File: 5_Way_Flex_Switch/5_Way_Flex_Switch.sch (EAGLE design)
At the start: 9 parts

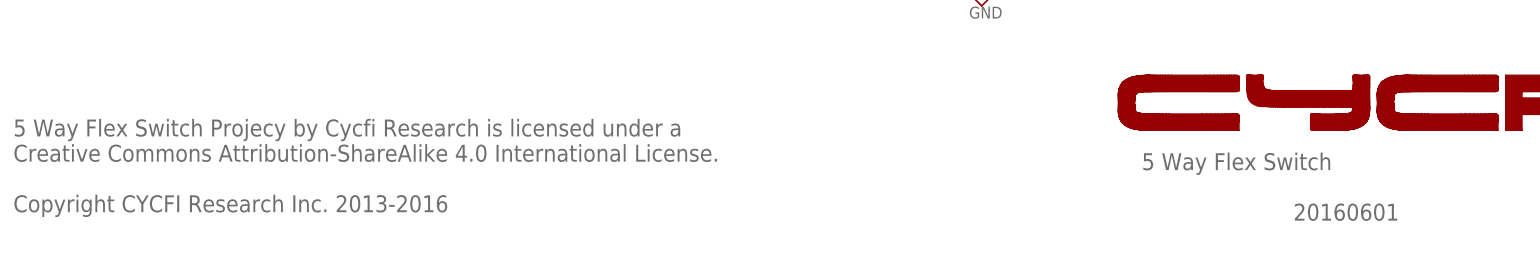
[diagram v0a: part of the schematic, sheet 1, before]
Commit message: *organize 5-waay switch and its configuration board(a and b) *update license date *remove red frame schem pdf files, change with black frame *update document number
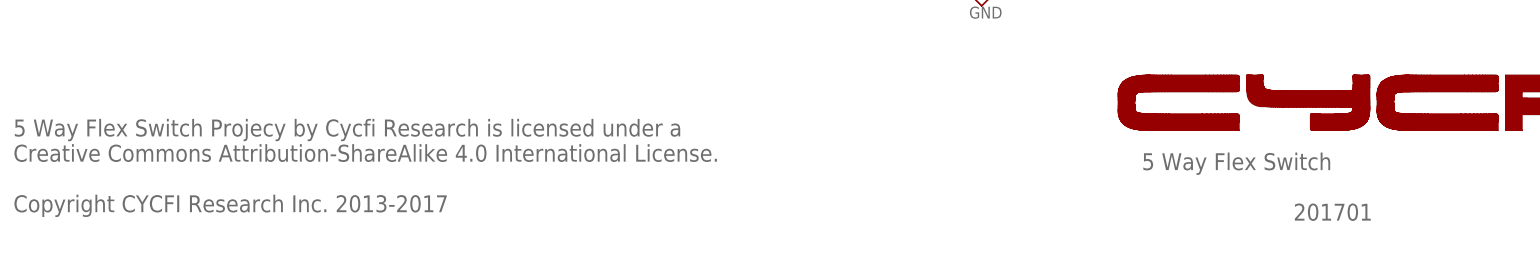
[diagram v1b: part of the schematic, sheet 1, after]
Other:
- note added: "201701"
- note added: "201702"
- note added: "5 Way Flex Switch Projecy by Cycfi Research is licensed under a Creative Commons Attribution-ShareAlike 4.0 International License. Copyright CYCFI Research Inc. 2013-2017"
- note removed: "2016037"
- note removed: "20160601"
- note removed: "5 Way Flex Switch Projecy by Cycfi Research is licensed under a Creative Commons Attribution-ShareAlike 4.0 International License. Copyright CYCFI Research Inc. 2013-2016"
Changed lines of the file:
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@@
 <text x="7.62" y="12.7" size="2.54" layer="95">5 Way Flex Switch Projecy by Cycfi Research is licensed under a
 Creative Commons Attribution-ShareAlike 4.0 International License.
-Copyright CYCFI Research Inc. 2013-2016</text>
-<text x="200.66" y="11.43" size="2.54" layer="95">20160601</text>
+Copyright CYCFI Research Inc. 2013-2017</text>
+<text x="200.66" y="11.43" size="2.54" layer="95">201701</text>
 <wire x1="192.47528125" y1="25.047221875" x2="190.115640625" y2="25.047221875" width="0" layer="94"/>
 <wire x1="190.115640625" y1="25.047221875" x2="188.10833125" y2="25.047225" width="0" layer="94"/>
@@
 <text x="7.62" y="12.7" size="2.54" layer="95">5 Way Flex Switch Projecy by Cycfi Research is licensed under a
 Creative Commons Attribution-ShareAlike 4.0 International License.
-Copyright CYCFI Research Inc. 2013-2016</text>
-<text x="200.66" y="11.43" size="2.54" layer="95">2016037</text>
+Copyright CYCFI Research Inc. 2013-2017</text>
+<text x="200.66" y="11.43" size="2.54" layer="95">201702</text>
 <wire x1="192.47528125" y1="25.047221875" x2="190.115640625" y2="25.047221875" width="0" layer="94"/>
 <wire x1="190.115640625" y1="25.047221875" x2="188.10833125" y2="25.047225" width="0" layer="94"/>

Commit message: * correct misspelled word
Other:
- note added: "5 Way Flex Switch Project by Cycfi Research is licensed under a Creative Commons Attribution-ShareAlike 4.0 International License. Copyright CYCFI Research Inc. 2013-2017"
- note removed: "5 Way Flex Switch Projecy by Cycfi Research is licensed under a Creative Commons Attribution-ShareAlike 4.0 International License. Copyright CYCFI Research Inc. 2013-2017"
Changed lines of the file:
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@@
 <text x="177.8" y="19.05" size="2.54" layer="95">5 Way Flex Switch</text>
 <text x="252.73" y="6.985" size="2.1844" layer="95">v1.2</text>
-<text x="7.62" y="12.7" size="2.54" layer="95">5 Way Flex Switch Projecy by Cycfi Research is licensed under a
+<text x="7.62" y="12.7" size="2.54" layer="95">5 Way Flex Switch Project by Cycfi Research is licensed under a
 Creative Commons Attribution-ShareAlike 4.0 International License.
 Copyright CYCFI Research Inc. 2013-2017</text>
@@
 <text x="177.8" y="19.05" size="2.54" layer="95">5 Way Flex Switch</text>
 <text x="252.73" y="6.985" size="2.1844" layer="95">v1.1</text>
-<text x="7.62" y="12.7" size="2.54" layer="95">5 Way Flex Switch Projecy by Cycfi Research is licensed under a
+<text x="7.62" y="12.7" size="2.54" layer="95">5 Way Flex Switch Project by Cycfi Research is licensed under a
 Creative Commons Attribution-ShareAlike 4.0 International License.
 Copyright CYCFI Research Inc. 2013-2017</text>
